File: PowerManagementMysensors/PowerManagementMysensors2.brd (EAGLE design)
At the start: 49.5 x 44.1 mm, 51 parts, among them IC2 AT25DF512C-SSHN-B, U1 LM8364BALMF20, U2 SI2399DS-T1-GE3, U3 SI2399DS-T1-GE3, U4 MCP1640BT-I/CHY, U5 TPS61222DCKT

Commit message: jst connector added
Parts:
- BATT: value M02PTH -> (none); device SparkFun-Connectors:1X02 -> adafruit:JST-PH-2-THM
- J10: device SparkFun-Connectors:1X05 -> SparkFun-Connectors:1X04
- J7: device SparkFun-Connectors:1X07 -> SparkFun-Connectors:1X05
- J8: device SparkFun-Connectors:1X04 -> SparkFun-Connectors:1X05
- J9: device SparkFun-Connectors:1X05 -> SparkFun-Connectors:1X07
- moved J3 17.8 mm to (47.6, 36.8)
- moved J8 16.3 mm to (37.5, 24.1), turned to 0 degrees
- moved J10 11.4 mm to (47.6, 19.1), turned to 180 degrees
- moved J7 7.18 mm to (37.5, 26.7)
- moved J9 7.18 mm to (32.4, 21.6)
- moved BATT 0.54 mm to (46.5, 4.57), turned to 90 degrees
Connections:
- net GND: now also J7.3, J9.5; no longer J7.5, J9.3
- net INT1: now also J10.4; no longer J3.4
- net INT2: now also J3.4; no longer J8.4
- net MISO: now also J9.4; no longer J7.4
- net MOSI: now also J9.3; no longer J7.3
- net SCK: now also J9.2; no longer J7.2
- net SCL: now also J7.1, J8.1; no longer J10.1, J9.1
- net SDA: now also J7.2, J8.2; no longer J10.2, J9.2
- net SPI_CSN: now also J9.1; no longer J7.1
- net V+5: now also J10.1, J7.5, J8.5, J9.7; no longer J10.5, J7.7, J8.1, J9.5
- net VCC_SENSORS: now also J10.2, J7.4, J8.4, J9.6; no longer J10.4, J7.6, J8.2, J9.4
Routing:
- net EN_BOOST: track 64.2 -> 65.3 mm
- net VIN: track 43.4 -> 42.7 mm
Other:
- board text removed: "VBAT"

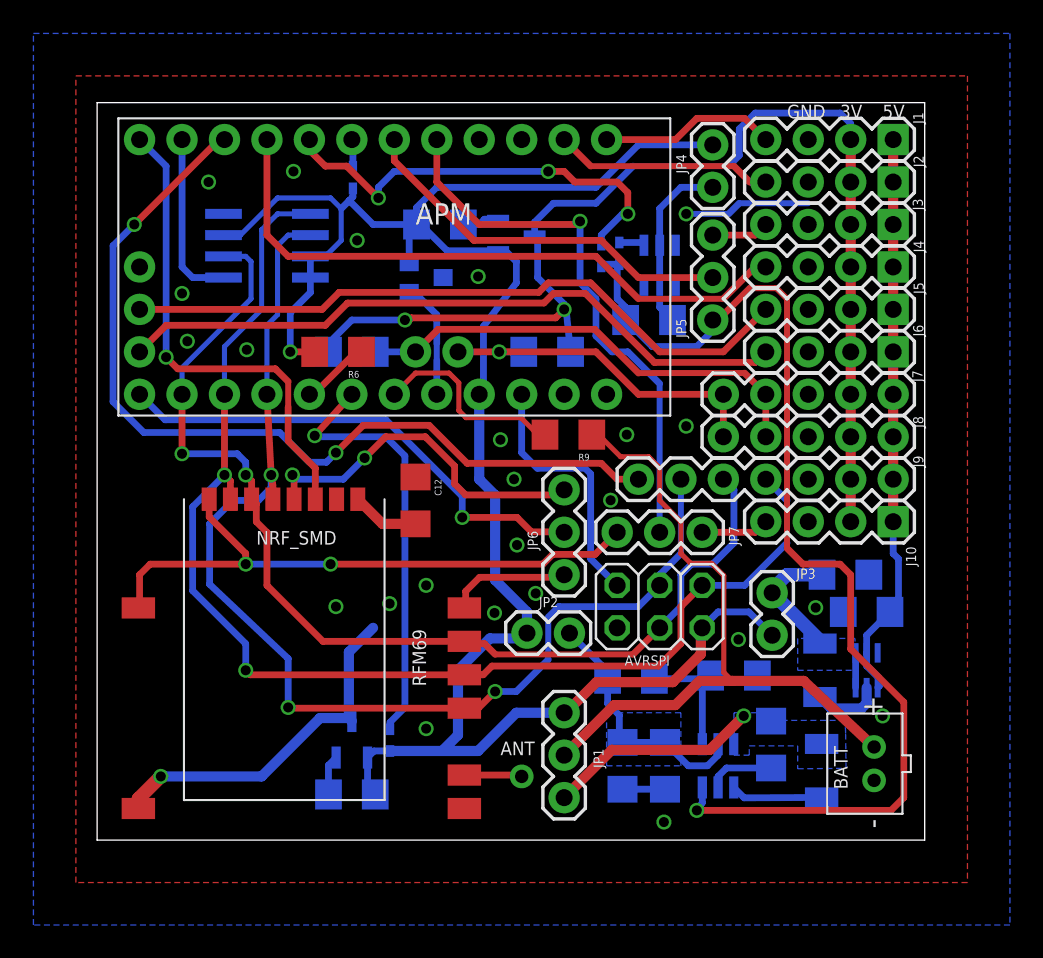
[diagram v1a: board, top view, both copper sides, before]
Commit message: changes
-res + zener to flash mem avoid fry
- dual schottky instead two single
- minor component ref changes
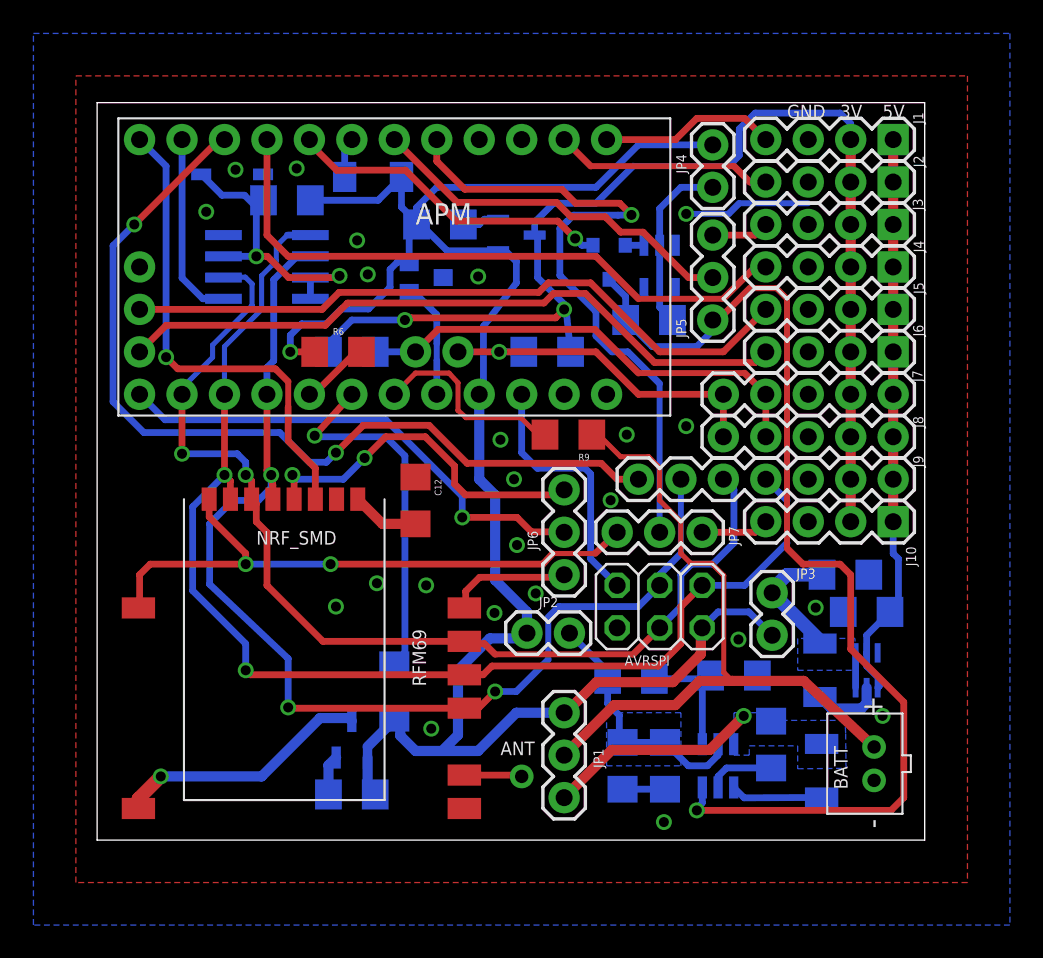
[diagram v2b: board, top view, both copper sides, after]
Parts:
- removed D4, D5: RB520S30T1G, diode:SOD523
- added D2: BZT52H-B3V6, adafruit:SOD-123
- added D6: BAT54C, zetex:SOT-23
- added R10: 47r-100r, SparkFun-Passives:1206
- D1, D3: value RB520S30T1G -> LL103A-GS08TR-ND; device diode:SOD523 -> semicon-smd-ipc:SOD80
- moved D3 29.4 mm to (17.8, 8.89), turned to 270 degrees
- moved D1 14.5 mm to (16.5, 39.7), turned to 180 degrees
- moved IC2 1.27 mm to (10.2, 34.3)
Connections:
- removed net N$6: APM.5, D1.A
- new net D5_ENBOOST: APM.5, D6.3
- new net N$16: D2.C, IC2.3, IC2.7, IC2.8, R10.1
- net EN_BOOST: now also D6.1; no longer D1.C, D3.C
- net EN_POWER: now also D1.1; no longer D5.C
- net EN_POWERRF: now also D3.1; no longer D4.C
- net GND: now also D2.A
- net N$5: now also D6.2; no longer D3.A
- net VCC: now also D1.2, D3.2, R10.2; no longer D4.A, D5.A, IC2.3, IC2.7, IC2.8
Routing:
- net N$6: track 26.4 -> 0.00 mm, vias 3 -> 0
- net D5_ENBOOST: track 0.00 -> 19.7 mm, vias 0 -> 1
- net N$16: track 0.00 -> 18.2 mm, vias 0 -> 2
- net D2: track 33.4 -> 40.1 mm
- net VCC_RF: track 21.4 -> 15.4 mm
- net EN_POWERRF: track 25.9 -> 21.9 mm
- net VCC: track 121.9 -> 119.6 mm
- net EN_BOOST: track 65.3 -> 63.5 mm
- net MISO: track 75.7 -> 74.1 mm
- net SCK: track 69.7 -> 68.2 mm
- net MOSI: track 64.7 -> 63.5 mm
- net FLASH_CSN: track 10.4 -> 11.3 mm
- net EN_POWER: track 1.65 -> 2.50 mm
- net D3: track 23.2 -> 22.5 mm
- net GND: vias 24 -> 23

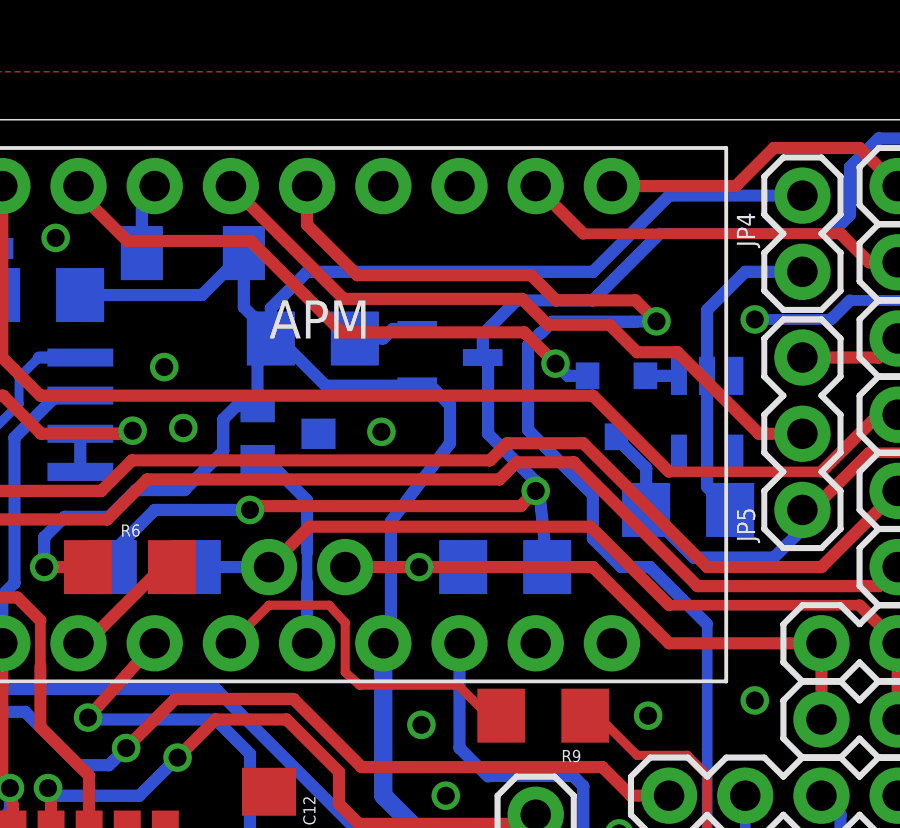
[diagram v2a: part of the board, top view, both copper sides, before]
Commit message: rst pin on arduino pro mini connected
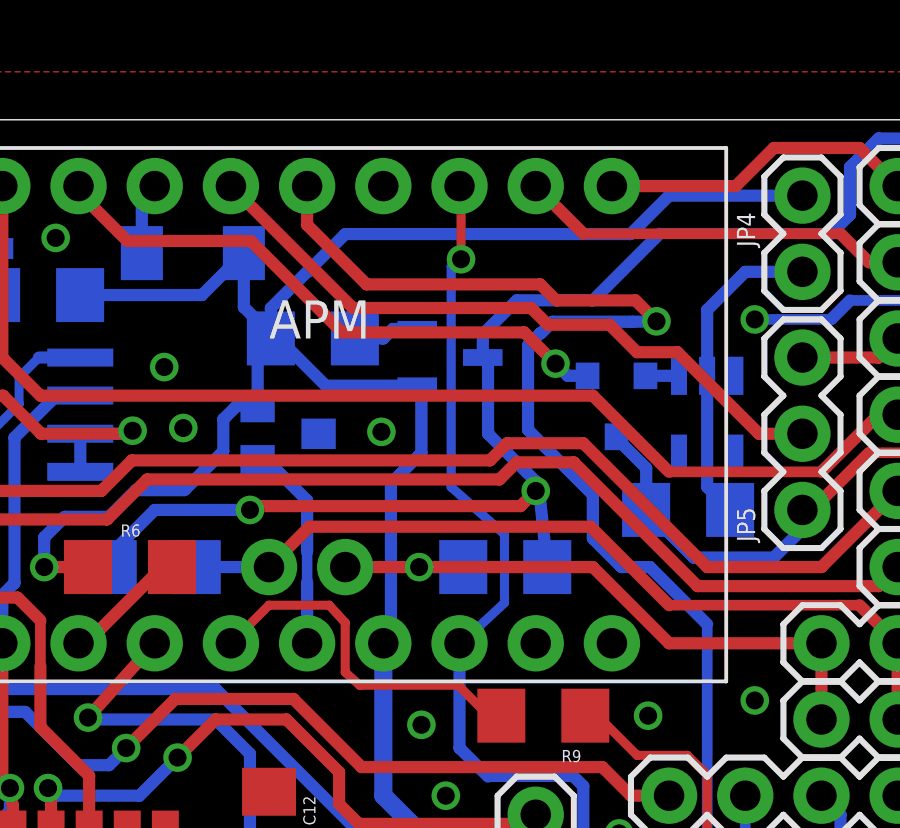
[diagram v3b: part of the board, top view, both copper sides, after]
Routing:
- net RST: track 15.5 -> 32.4 mm, vias 0 -> 1
- net VCC: track 119.6 -> 118.7 mm
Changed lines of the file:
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@@
 <wire x1="19.1105" y1="36.83" x2="19.1105" y2="37.843" width="0.4064" layer="16"/>
 <wire x1="19.1105" y1="36.83" x2="18.5928" y2="36.83" width="0.4064" layer="16"/>
-<wire x1="23.114" y1="30.734" x2="25.0825" y2="33.3375" width="0.4064" layer="16"/>
-<wire x1="25.0825" y1="33.3375" x2="25.0825" y2="34.6075" width="0.4064" layer="16"/>
-<wire x1="25.0825" y1="34.6075" x2="24.4475" y2="35.2425" width="0.4064" layer="16"/>
-<wire x1="24.4475" y1="35.2425" x2="24.003" y2="35.2425" width="0.4064" layer="16"/>
 <wire x1="24.003" y1="35.2425" x2="23.9903" y2="35.2552" width="0.4064" layer="16"/>
 <wire x1="23.9903" y1="35.2552" x2="20.9423" y2="35.2552" width="0.4064" layer="16"/>
@@
 <wire x1="19.428" y1="36.5125" x2="19.1105" y2="36.83" width="0.4064" layer="16"/>
 <wire x1="19.1105" y1="37.843" x2="20.32" y2="39.0525" width="0.4064" layer="16"/>
-<wire x1="20.32" y1="39.0525" x2="29.845" y2="39.0525" width="0.4064" layer="16"/>
-<wire x1="29.845" y1="39.0525" x2="32.385" y2="41.5925" width="0.4064" layer="16"/>
 <wire x1="25.7175" y1="12.3825" x2="25.7175" y2="13.6525" width="0.6096" layer="16"/>
 <wire x1="25.7175" y1="13.6525" x2="23.8125" y2="15.5575" width="0.6096" layer="16"/>
@@
 <wire x1="21.59" y1="10.16" x2="21.59" y2="6.285" width="0.6096" layer="16"/>
 <wire x1="21.59" y1="6.285" x2="20.6375" y2="5.3325" width="0.6096" layer="16"/>
-<wire x1="23.114" y1="26.924" x2="23.114" y2="30.734" width="0.4064" layer="16"/>
+<wire x1="23.114" y1="26.924" x2="23.114" y2="32.004" width="0.4064" layer="16"/>
 <wire x1="27.94" y1="7.62" x2="28.0416" y2="7.62" width="0.6096" layer="1"/>
 <wire x1="28.0416" y1="7.62" x2="29.8704" y2="9.4488" width="0.6096" layer="1"/>
@@
 <wire x1="16.1798" y1="4.9403" x2="16.1798" y2="5.5898" width="0.4064" layer="16"/>
 <wire x1="16.1798" y1="5.5898" x2="17.78" y2="7.19" width="0.6096" layer="16"/>
+<wire x1="23.114" y1="32.004" x2="24.13" y2="33.02" width="0.4064" layer="16"/>
+<wire x1="24.13" y1="33.02" x2="24.13" y2="35.1155" width="0.4064" layer="16"/>
+<wire x1="24.13" y1="35.1155" x2="23.9903" y2="35.2552" width="0.4064" layer="16"/>
+<wire x1="20.32" y1="39.0525" x2="20.3327" y2="39.0525" width="0.4064" layer="16"/>
+<wire x1="20.3327" y1="39.0525" x2="21.59" y2="40.3098" width="0.4064" layer="16"/>
+<wire x1="21.59" y1="40.3098" x2="31.1023" y2="40.3098" width="0.4064" layer="16"/>
+<wire x1="31.1023" y1="40.3098" x2="32.385" y2="41.5925" width="0.4064" layer="16"/>
 </signal>
 <signal name="N$1">
@@
 <wire x1="26.3525" y1="22.225" x2="25.4" y2="23.1775" width="0.4064" layer="16"/>
 <wire x1="25.4" y1="23.1775" x2="25.4" y2="26.67" width="0.4064" layer="16"/>
-<wire x1="25.4" y1="26.67" x2="25.4" y2="41.91" width="0" layer="19" extent="1-1"/>
+<wire x1="25.4" y1="26.67" x2="25.4508" y2="26.67" width="0.3048" layer="16"/>
+<wire x1="25.4508" y1="26.67" x2="26.8986" y2="28.0162" width="0.3048" layer="16"/>
+<wire x1="26.8986" y1="28.0162" x2="26.8986" y2="30.3022" width="0.3048" layer="16"/>
+<wire x1="26.8986" y1="30.3022" x2="25.1206" y2="31.877" width="0.3048" layer="16"/>
+<wire x1="25.1206" y1="31.877" x2="25.1206" y2="39.243" width="0.3048" layer="16"/>
+<wire x1="25.1206" y1="39.243" x2="25.4508" y2="39.4716" width="0.3048" layer="16"/>
+<via x="25.4508" y="39.4716" extent="1-16" drill="0.6" shape="square"/>
+<wire x1="25.4508" y1="39.4716" x2="25.4508" y2="41.8592" width="0.3048" layer="1"/>
+<wire x1="25.4508" y1="41.8592" x2="25.4" y2="41.91" width="0.3048" layer="1"/>
 </signal>
 <signal name="TX">
@@
 <wire x1="27.686" y1="36.6014" x2="28.0924" y2="37.0078" width="0.4064" layer="16"/>
 <wire x1="20.32" y1="41.91" x2="20.32" y2="40.6146" width="0.4064" layer="1"/>
-<wire x1="20.32" y1="40.6146" x2="21.9964" y2="38.9382" width="0.4064" layer="1"/>
+<wire x1="20.32" y1="40.6146" x2="22.3012" y2="38.6334" width="0.4064" layer="1"/>
 <wire x1="28.0924" y1="37.0078" x2="28.1178" y2="37.0078" width="0.4064" layer="16"/>
 <wire x1="28.1178" y1="37.0078" x2="28.4988" y2="37.3888" width="0.4064" layer="16"/>
 <wire x1="28.4988" y1="37.3888" x2="31.1658" y2="37.3888" width="0.4064" layer="16"/>
 <wire x1="31.1658" y1="37.3888" x2="31.9659" y2="37.4015" width="0.4064" layer="16"/>
-<wire x1="21.9964" y1="38.9382" x2="27.7876" y2="38.9382" width="0.4064" layer="1"/>
-<wire x1="27.7876" y1="38.9382" x2="28.6258" y2="38.1" width="0.4064" layer="1"/>
+<wire x1="22.3012" y1="38.6334" x2="28.0924" y2="38.6334" width="0.4064" layer="1"/>
+<wire x1="28.0924" y1="38.6334" x2="28.6258" y2="38.1" width="0.4064" layer="1"/>
 <wire x1="28.6258" y1="38.1" x2="31.2674" y2="38.1" width="0.4064" layer="1"/>
 <wire x1="31.2674" y1="38.1" x2="31.9659" y2="37.4015" width="0.4064" layer="1"/>
@@
 <wire x1="31.3182" y1="36.3728" x2="30.4038" y2="37.2872" width="0.4064" layer="1"/>
 <wire x1="30.4038" y1="37.2872" x2="28.3464" y2="37.2872" width="0.4064" layer="1"/>
-<wire x1="28.3464" y1="37.2872" x2="27.4828" y2="38.1508" width="0.4064" layer="1"/>
-<wire x1="27.4828" y1="38.1508" x2="21.5392" y2="38.1508" width="0.4064" layer="1"/>
-<wire x1="21.5392" y1="38.1508" x2="17.78" y2="41.91" width="0.4064" layer="1"/>
+<wire x1="28.3464" y1="37.2872" x2="27.7876" y2="37.846" width="0.4064" layer="1"/>
+<wire x1="27.7876" y1="37.846" x2="21.844" y2="37.846" width="0.4064" layer="1"/>
+<wire x1="21.844" y1="37.846" x2="17.78" y2="41.91" width="0.4064" layer="1"/>
 </signal>
 <signal name="N$11">
